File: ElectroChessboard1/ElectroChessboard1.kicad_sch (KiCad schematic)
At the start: 0 parts

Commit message: Start + Halls
Created base + placed all hall sensors
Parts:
- added C4: GCM21B5G1H103FA16L, GCM21, symbol SamacSys_Parts:GCM21B5G1H103FA16L
- added C5: KAM21BR71H104JT, CAPC2012X94N, symbol SamacSys_Parts:KAM21BR71H104JT
- added D3: 1N4148, Diode_THT:D_DO-35_SOD27_P7.62mm_Horizontal, symbol Diode:1N4148
- added R1: ERA-6ARW512V, ERA6AEB101V, symbol SamacSys_Parts:ERA-6ARW512V
- added U1: ATmega2560-16A, Package_QFP:TQFP-100_14x14mm_P0.5mm, symbol MCU_Microchip_ATmega:ATmega2560-16A
- added Y2: XO57CRECNA16M, XO57CRECNA16M, symbol SamacSys_Parts:XO57CRECNA16M
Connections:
- new net: D3.2 (A), R1.2, U1.30 (~{RESET})
- new net: U1.34 (XTAL1), Y2.3 (OUTPUT)
- new net: C5.2, U1.98 (AREF)
- new net: C4.2, Y2.1 (TRI-STATE)
- new net SafeGND: C5.1, U1.11 (GND), U1.32 (GND), U1.62 (GND), U1.81 (GND), U1.99 (GND), Y2.2 (GND)
- new net SafeVCC: C4.1, D3.1 (K), R1.1, U1.10 (VCC), U1.100 (AVCC), U1.31 (VCC), U1.61 (VCC), U1.80 (VCC), Y2.4 (VDD)
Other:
- added sheet BoardHalls1 (board.kicad_sch)
- added sheet BoardHalls2 (BoardHalls2.kicad_sch)
- added sheet BoardHalls3 (BoardHalls3.kicad_sch)
- added sheet BoardHalls4 (BoardHalls4.kicad_sch)
- added sheet BoardLEDs (BoardLEDs.kicad_sch)
- added sheet PowerInput (PowerInput.kicad_sch)
- note added: "// Analog Input ADC0 Pin = PF0 ADC1 Pin = PF1 ADC2 Pin = PF2 ADC3 Pin = PF3 ADC4 Pin = PF4 ADC5 Pin = PF5 ADC6 Pin = PF6 ADC7 Pin = PF7 ADC8 Pin = PK0 ADC9 Pin = PK1 ADC10 Pin = PK2 ADC11 Pin = PK3 ADC12 Pin = PK4 ADC13 Pin = PK5 ADC14 Pin = PK6 ADC15 Pin = PK7 // Digital pins D0 Pin = PE0 D1 Pin = PE1 D2 Pin = PE4 D3 Pin = PE5 D4 Pin = PG5 D5 Pin = PE3 D6 Pin = PH3 D7 Pin = PH4 D8 Pin = PH5 D9 P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"
- note added: "Może być <=20 MHz Zastąpić oscylatorem jeśli element niedostępny"
- note added: "Sprawdzić, czy na pewno do GND aby analog inputs działało, zweryfikować na JEDEN Board"
- note added: "TODO: Podłącz ISP"

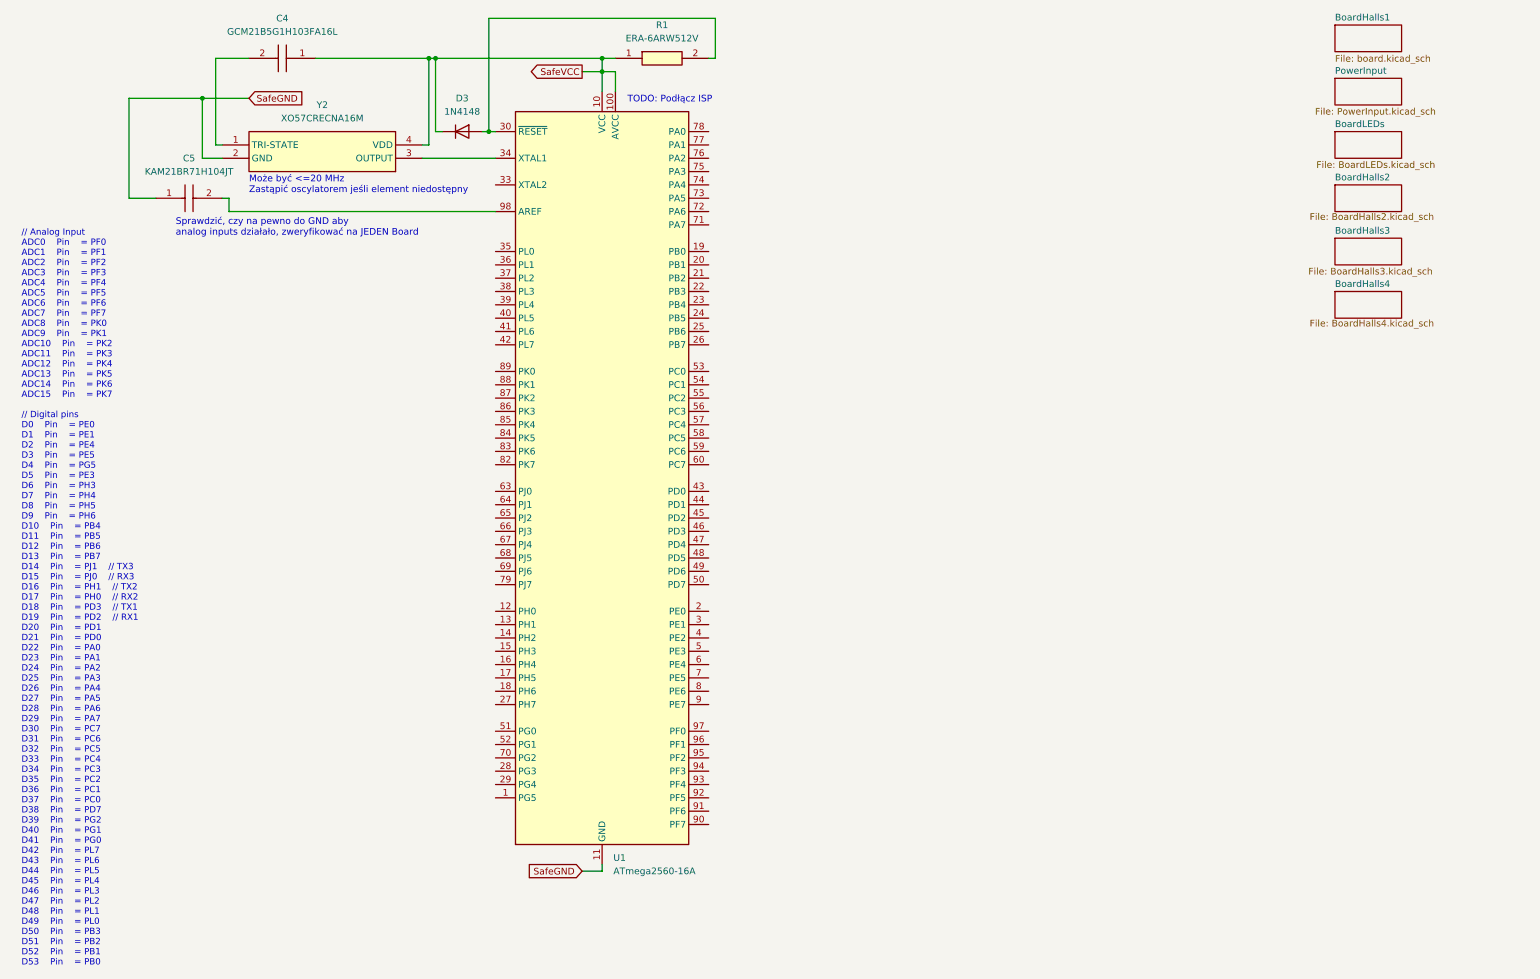
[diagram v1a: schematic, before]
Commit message: LEDs added
Wired Hall sensors and LEDs
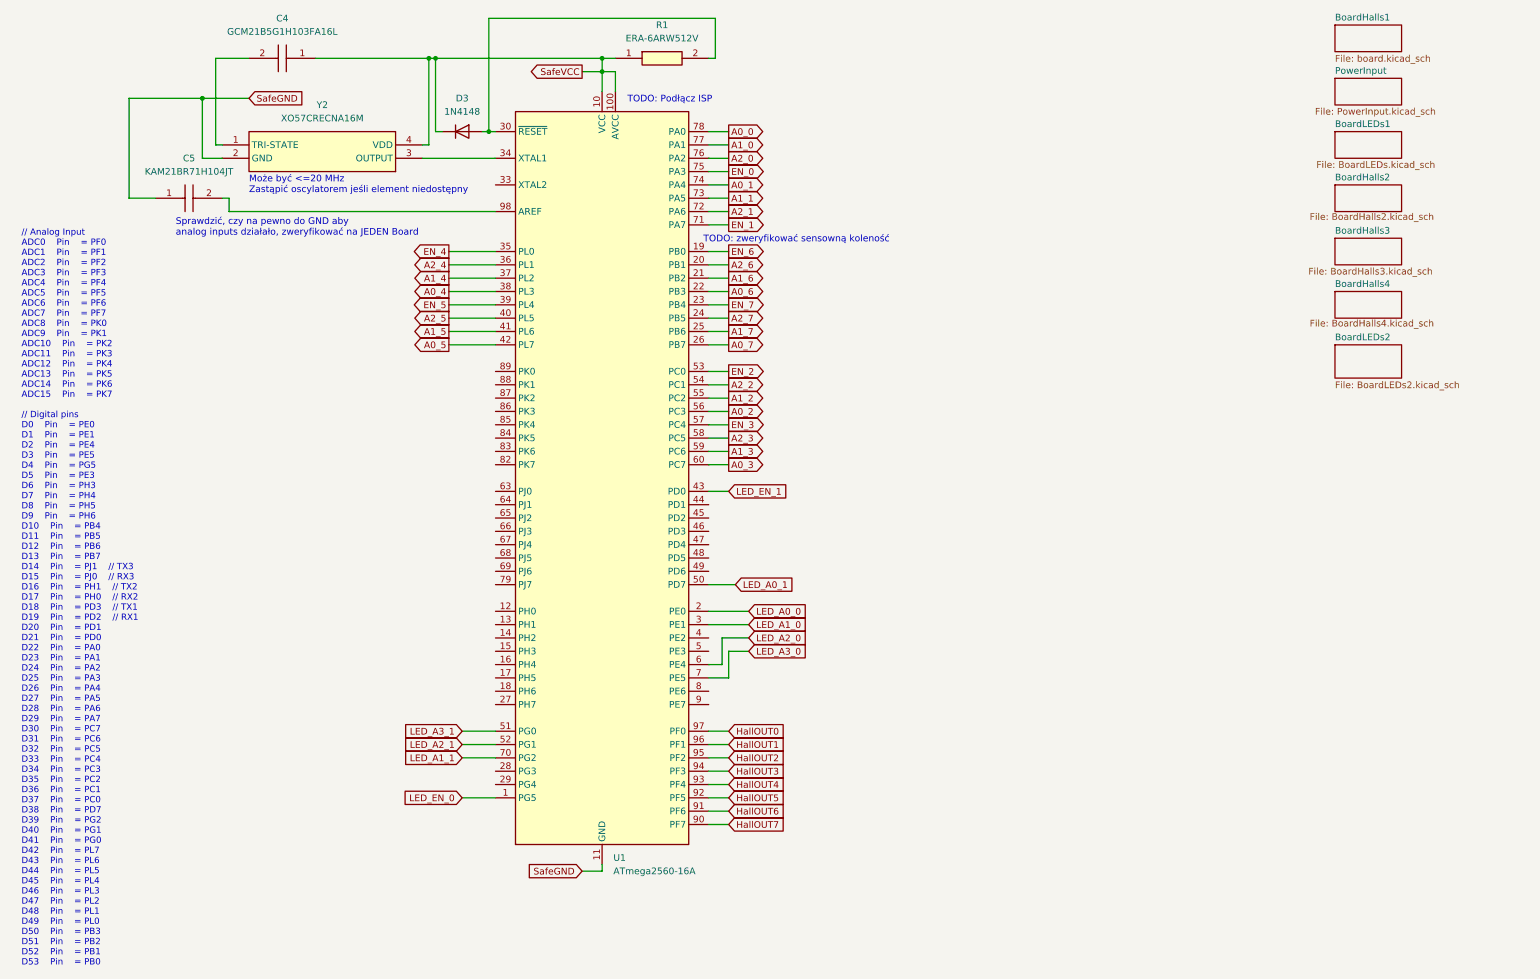
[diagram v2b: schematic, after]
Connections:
- net LED_EN_0: now reaches U1.1 (PG5)
- net EN_6: now reaches U1.19 (PB0)
- net LED_A0_0: now reaches U1.2 (PE0)
- net A2_6: now reaches U1.20 (PB1)
- net A1_6: now reaches U1.21 (PB2)
- net A0_6: now reaches U1.22 (PB3)
- net EN_7: now reaches U1.23 (PB4)
- net A2_7: now reaches U1.24 (PB5)
- net A1_7: now reaches U1.25 (PB6)
- net A0_7: now reaches U1.26 (PB7)
- net LED_A1_0: now reaches U1.3 (PE1)
- net EN_4: now reaches U1.35 (PL0)
- net A2_4: now reaches U1.36 (PL1)
- net A1_4: now reaches U1.37 (PL2)
- net A0_4: now reaches U1.38 (PL3)
- net EN_5: now reaches U1.39 (PL4)
- net A2_5: now reaches U1.40 (PL5)
- net A1_5: now reaches U1.41 (PL6)
- net A0_5: now reaches U1.42 (PL7)
- net LED_EN_1: now reaches U1.43 (PD0)
- net LED_A0_1: now reaches U1.50 (PD7)
- net LED_A3_1: now reaches U1.51 (PG0)
- net LED_A2_1: now reaches U1.52 (PG1)
- net EN_2: now reaches U1.53 (PC0)
- net A2_2: now reaches U1.54 (PC1)
- net A1_2: now reaches U1.55 (PC2)
- net A0_2: now reaches U1.56 (PC3)
- net EN_3: now reaches U1.57 (PC4)
- net A2_3: now reaches U1.58 (PC5)
- net A1_3: now reaches U1.59 (PC6)
- net LED_A2_0: now reaches U1.6 (PE4)
- net A0_3: now reaches U1.60 (PC7)
- net LED_A3_0: now reaches U1.7 (PE5)
- net LED_A1_1: now reaches U1.70 (PG2)
- net EN_1: now reaches U1.71 (PA7)
- net A2_1: now reaches U1.72 (PA6)
- net A1_1: now reaches U1.73 (PA5)
- net A0_1: now reaches U1.74 (PA4)
- net EN_0: now reaches U1.75 (PA3)
- net A2_0: now reaches U1.76 (PA2)
- net A1_0: now reaches U1.77 (PA1)
- net A0_0: now reaches U1.78 (PA0)
- net HallOUT7: now reaches U1.90 (PF7)
- net HallOUT6: now reaches U1.91 (PF6)
- net HallOUT5: now reaches U1.92 (PF5)
- net HallOUT4: now reaches U1.93 (PF4)
- net HallOUT3: now reaches U1.94 (PF3)
- net HallOUT2: now reaches U1.95 (PF2)
- net HallOUT1: now reaches U1.96 (PF1)
- net HallOUT0: now reaches U1.97 (PF0)
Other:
- sheet BoardLEDs renamed BoardLEDs1
- added sheet BoardLEDs2 (BoardLEDs2.kicad_sch)
- note added: "TODO: zweryfikować sensowną koleność"

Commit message: Added but not connected yet SD Card pins and RTC
.
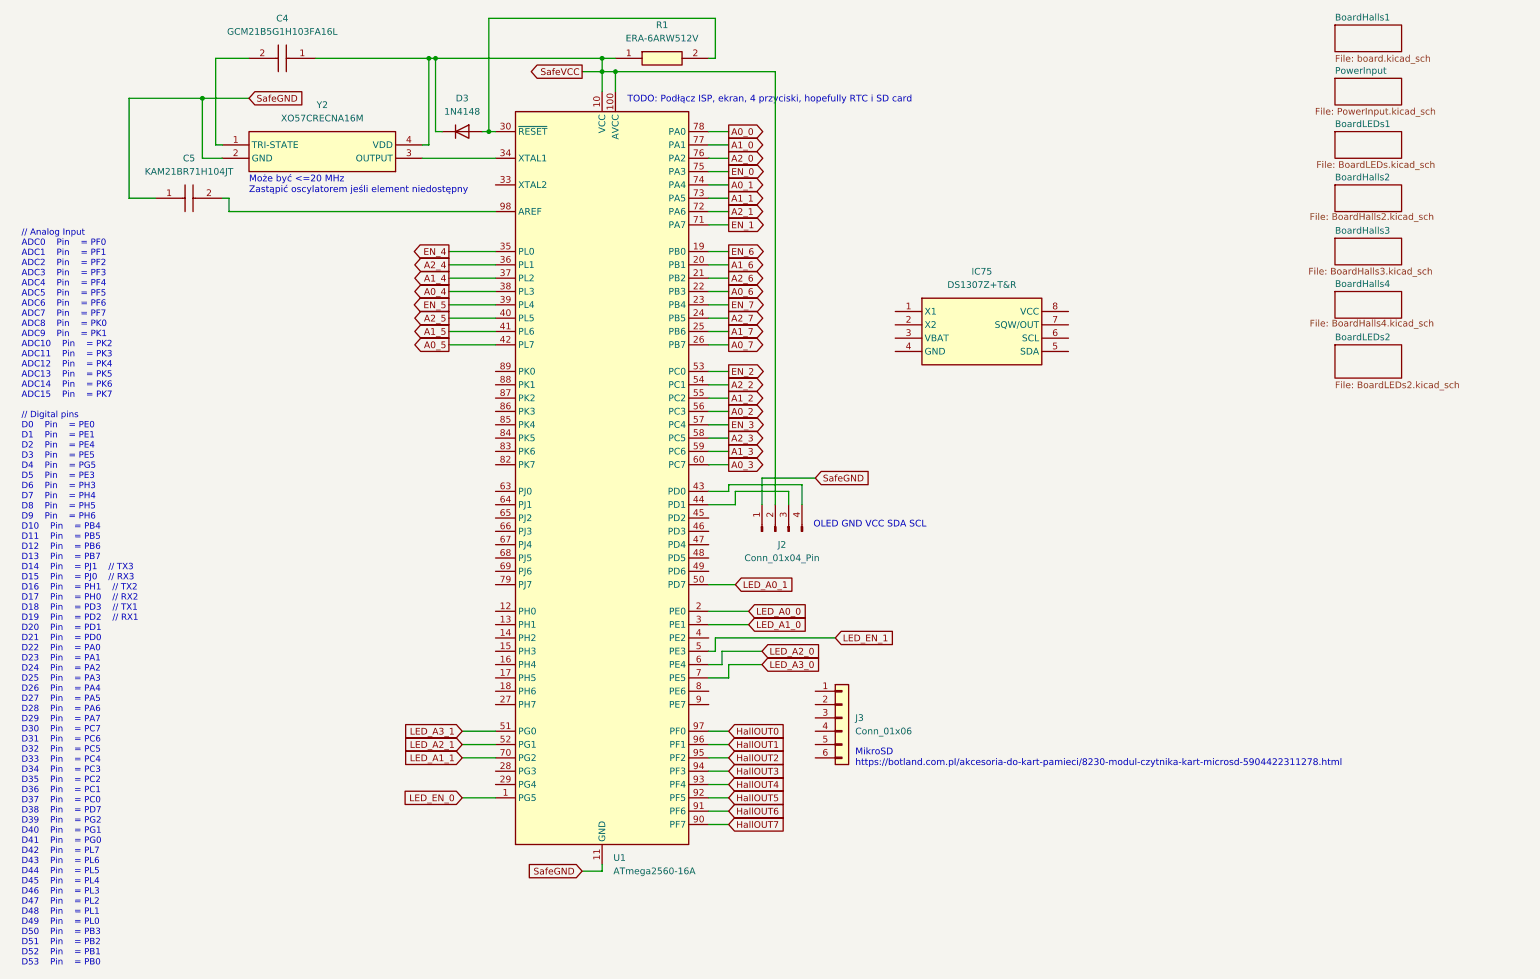
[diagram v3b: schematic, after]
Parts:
- added IC75: DS1307Z+T&R, SOIC127P600X175-8N, symbol SamacSys_Parts:DS1307Z+T&R
- added J2: Conn_01x04_Pin, Connector_PinHeader_1.00mm:PinHeader_1x04_P1.00mm_Vertical, symbol Connector:Conn_01x04_Pin
- added J3: Conn_01x06, Connector_Harwin:Harwin_M20-89006xx_1x06_P2.54mm_Horizontal, symbol Connector_Generic:Conn_01x06
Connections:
- net A1_6: now also U1.20 (PB1); no longer U1.21 (PB2)
- net A2_6: now also U1.21 (PB2); no longer U1.20 (PB1)
- net LED_EN_1: now also U1.5 (PE3); no longer U1.43 (PD0)
- net SafeGND: now also J2.1 (Pin_1)
- net SafeVCC: now also J2.2 (Pin_2)
- net at U1.44 (PD1): now also J2.3 (Pin_3)
- new net: J2.4 (Pin_4), U1.43 (PD0)
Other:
- note added: "MikroSD https://botland.com.pl/akcesoria-do-kart-pamieci/8230-modul-czytnika-kart-microsd-5904422311278.html"
- note added: "OLED GND VCC SDA SCL"
- note added: "TODO: Podłącz ISP, ekran, 4 przyciski, hopefully RTC i SD card"
- note removed: "Sprawdzić, czy na pewno do GND aby analog inputs działało, zweryfikować na JEDEN Board"
- note removed: "TODO: Podłącz ISP"
- note removed: "TODO: zweryfikować sensowną koleność"

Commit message: Schematic practically done (V0)
Only requires pin verification and setting footprints.

PDFs and image added in this commit all come from arduino.cc and microchip.com
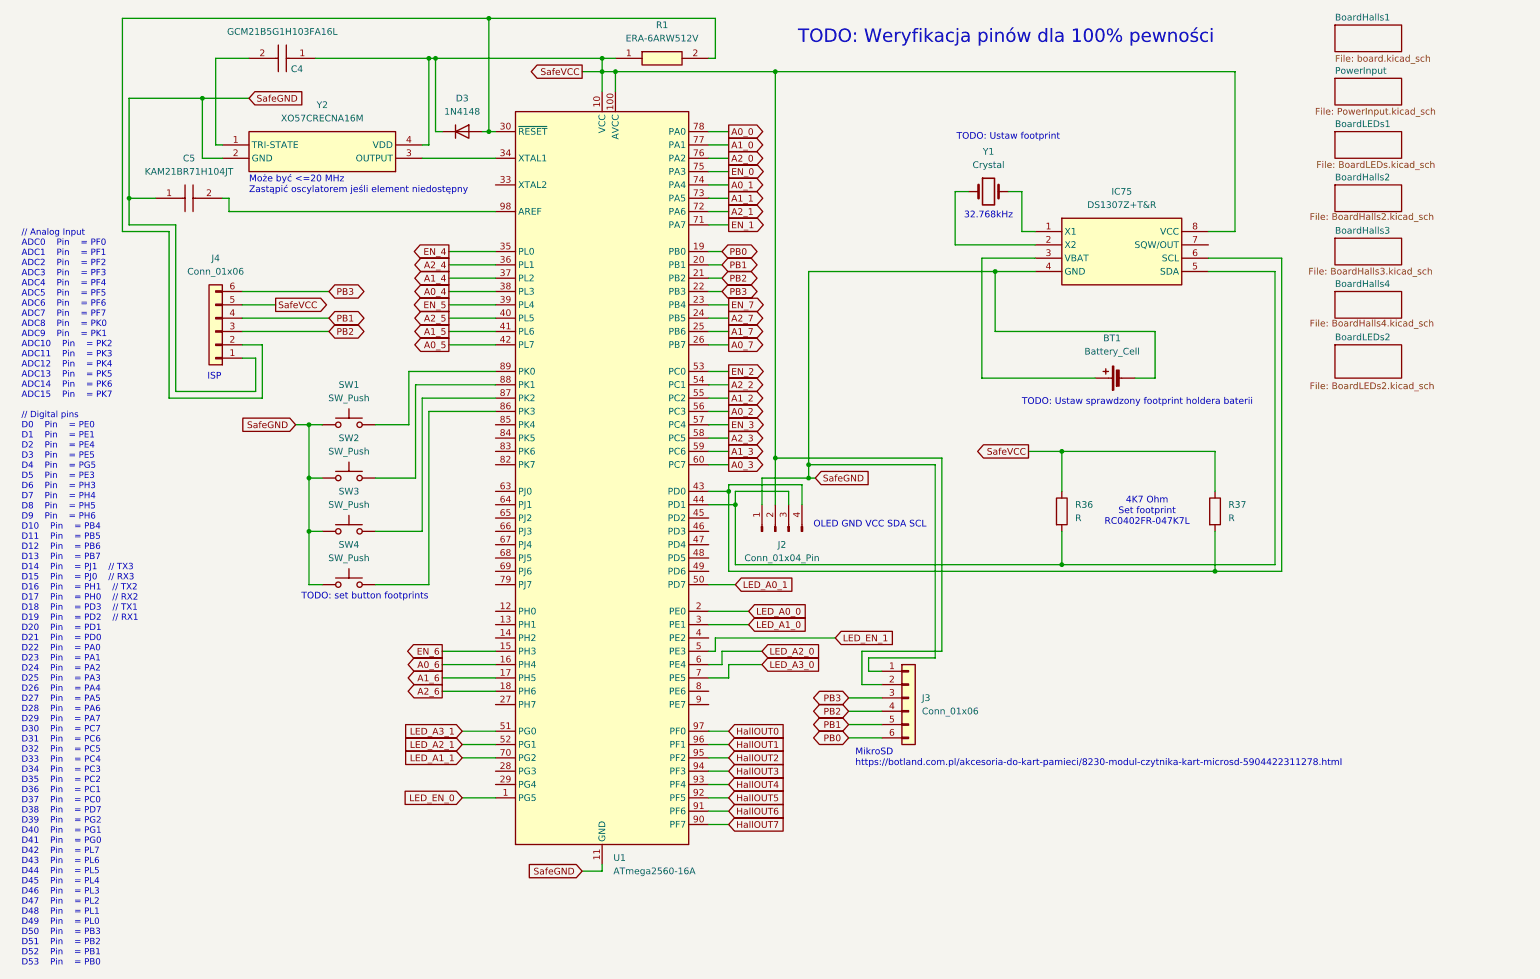
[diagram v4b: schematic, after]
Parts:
- added BT1: Battery_Cell, symbol Device:Battery_Cell
- added J4: Conn_01x06, Connector_Harwin:Harwin_M20-89006xx_1x06_P2.54mm_Horizontal, symbol Connector_Generic:Conn_01x06
- added R36, R37: R, symbol Device:R
- added SW1, SW2, SW3, SW4: SW_Push, symbol Switch:SW_Push
- added Y1: Crystal, symbol Device:Crystal
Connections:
- net A0_6: now also U1.16 (PH4); no longer U1.22 (PB3)
- net A1_6: now also U1.17 (PH5); no longer U1.20 (PB1)
- net A2_6: now also U1.18 (PH6); no longer U1.21 (PB2)
- net EN_6: now also U1.15 (PH3); no longer U1.19 (PB0)
- net SafeGND: now also IC75.4 (GND), J3.1 (Pin_1), BT1.2 (-), J4.1 (Pin_1), SW1.1, SW2.1, SW3.1, SW4.1
- net SafeVCC: now also IC75.8 (VCC), J3.2 (Pin_2), J4.5 (Pin_5), R36.1, R37.1
- net at J2.3 (Pin_3), U1.44 (PD1): now also IC75.5 (SDA), R36.2
- net at J2.4 (Pin_4), U1.43 (PD0): now also IC75.6 (SCL), R37.2
- net at D3.2 (A), R1.2, U1.30 (~{RESET}): now also J4.2 (Pin_2)
- net at U1.86 (PK3): now also SW4.2
- net at U1.87 (PK2): now also SW3.2
- net at U1.88 (PK1): now also SW2.2
- net at U1.89 (PK0): now also SW1.2
- net at IC75.1 (X1): now also Y1.2
- net at IC75.2 (X2): now also Y1.1
- net at IC75.3 (VBAT): now also BT1.1 (+)
- net PB3: now reaches J3.3 (Pin_3)
- net PB3: now also U1.22 (PB3), J4.6 (Pin_6)
- net PB2: now reaches J3.4 (Pin_4)
- net PB2: now also U1.21 (PB2), J4.3 (Pin_3)
- net PB1: now reaches J3.5 (Pin_5)
- net PB1: now also U1.20 (PB1), J4.4 (Pin_4)
- net PB0: now reaches J3.6 (Pin_6)
- net PB0: now also U1.19 (PB0)
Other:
- note added: "32.768kHz"
- note added: "4K7 Ohm Set footprint RC0402FR-047K7L"
- note added: "ISP"
- note added: "TODO: Ustaw footprint"
- note added: "TODO: Ustaw sprawdzony footprint holdera baterii"
- note added: "TODO: Weryfikacja pinów dla 100% pewności"
- note added: "TODO: set button footprints"
- note removed: "TODO: Podłącz ISP, ekran, 4 przyciski, hopefully RTC i SD card"
- moved on the sheet: IC75, J3
